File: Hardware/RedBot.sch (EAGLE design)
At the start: 67 parts, among them U1 ATMEGA328P, U2 TB6612FNG, U3 MIC5219 5V, U4 MIC5219 3.3V, U5 FT232RLSSOP, U6 7408SE, Y1 16MHz

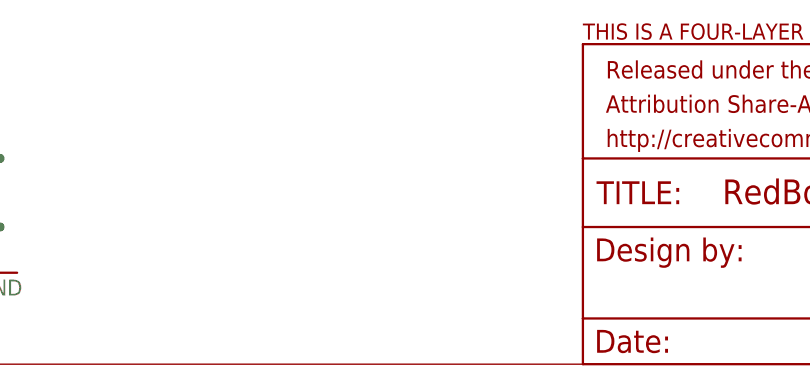
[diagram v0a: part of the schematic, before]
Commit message: Added RedBot logo
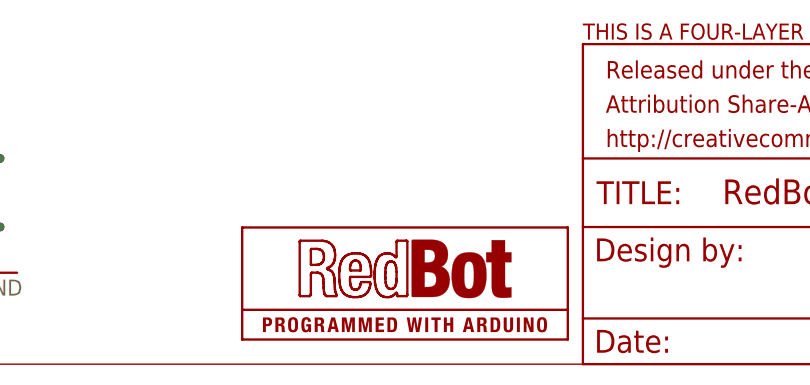
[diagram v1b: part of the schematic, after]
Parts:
- added U$23: REDBOT_LOGO, SparkFun-Aesthetics:REDBOT_LOGO
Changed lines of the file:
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@@
 <part name="S5" library="SparkFun-Electromechanical" deviceset="TAC_SWITCH" device="SMD"/>
 <part name="GND12" library="SparkFun-Aesthetics" deviceset="GND" device=""/>
+<part name="U$23" library="SparkFun-Aesthetics" deviceset="REDBOT_LOGO" device=""/>
 </parts>
 <sheets>
@@
 <instance part="S5" gate="S" x="309.88" y="93.98" rot="R90"/>
 <instance part="GND12" gate="1" x="309.88" y="83.82"/>
+<instance part="U$23" gate="G$1" x="266.7" y="2.54"/>
 </instances>
 <busses>

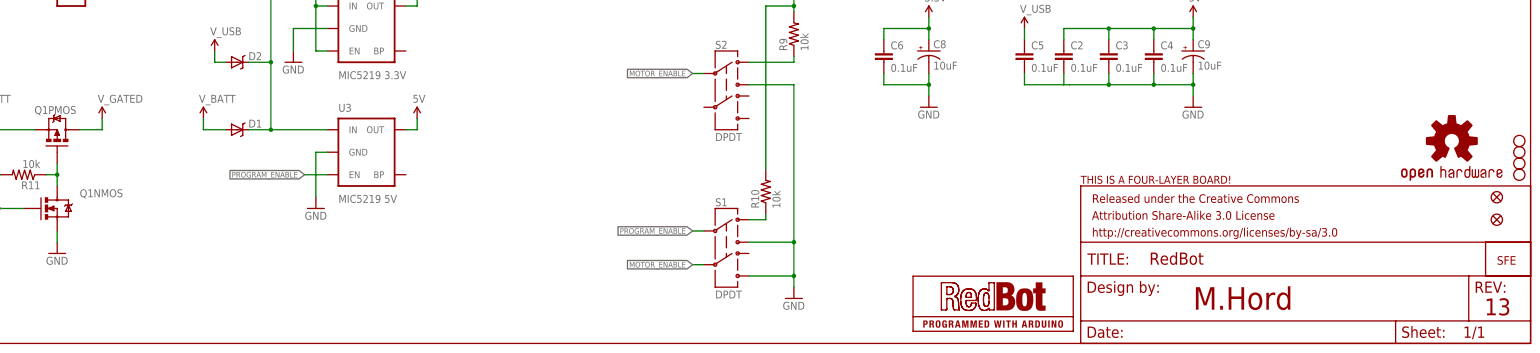
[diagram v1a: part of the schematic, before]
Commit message: Added PTC to V_GATED
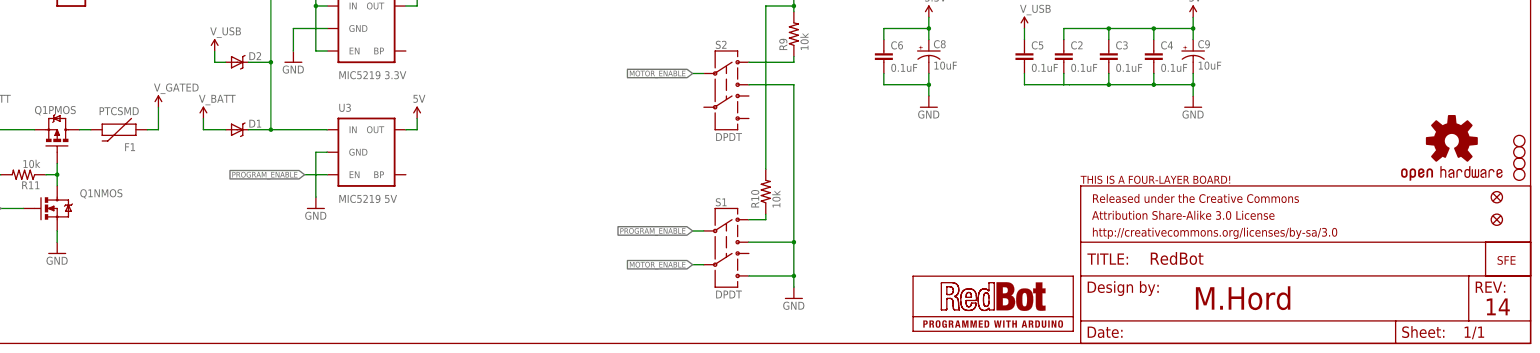
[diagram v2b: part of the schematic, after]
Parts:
- added F1: PTCSMD, SparkFun-PowerIC:PTCSMD
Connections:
- new net N$9: F1.2, Q1PMOS.D
- net V_GATED: now also F1.1; no longer Q1PMOS.D
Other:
- note added: "14"
- note removed: "13"
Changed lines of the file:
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@@
 <part name="GND12" library="SparkFun-Aesthetics" deviceset="GND" device=""/>
 <part name="U$23" library="SparkFun-Aesthetics" deviceset="REDBOT_LOGO" device=""/>
+<part name="F1" library="SparkFun-PowerIC" deviceset="PTC" device="SMD"/>
 </parts>
 <sheets>
@@
 <wire x1="0" y1="254" x2="0" y2="0" width="0.1524" layer="94"/>
 <text x="330.2" y="7.62" size="5.08" layer="94">M.Hord</text>
-<text x="395.986" y="6.35" size="3.81" layer="94">13</text>
+<text x="395.986" y="6.35" size="3.81" layer="94">14</text>
 </plain>
 <instances>
@@
 <instance part="U$18" gate="G$1" x="55.88" y="50.8"/>
 <instance part="GND20" gate="1" x="132.08" y="30.48"/>
-<instance part="V_GATE1" gate="G$1" x="83.82" y="50.8"/>
+<instance part="V_GATE1" gate="G$1" x="96.52" y="53.34"/>
 <instance part="U$4" gate="G$1" x="106.68" y="50.8"/>
 <instance part="JP16" gate="G$1" x="15.24" y="22.86"/>
@@
 <instance part="GND12" gate="1" x="309.88" y="83.82"/>
 <instance part="U$23" gate="G$1" x="266.7" y="2.54"/>
+<instance part="F1" gate="G$1" x="88.9" y="48.26" rot="R180"/>
 </instances>
 <busses>
@@
 <segment>
 <pinref part="V_GATE1" gate="G$1" pin="V_BATT"/>
-<wire x1="83.82" y1="50.8" x2="83.82" y2="48.26" width="0.1524" layer="91"/>
-<pinref part="Q1" gate="PMOS" pin="D"/>
-<wire x1="78.74" y1="48.26" x2="83.82" y2="48.26" width="0.1524" layer="91"/>
+<wire x1="96.52" y1="48.26" x2="96.52" y2="53.34" width="0.1524" layer="91"/>
+<pinref part="F1" gate="G$1" pin="1"/>
+<wire x1="93.98" y1="48.26" x2="96.52" y2="48.26" width="0.1524" layer="91"/>
 </segment>
 <segment>
@@
 </segment>
 </net>
+<net name="N$9" class="0">
+<segment>
+<pinref part="F1" gate="G$1" pin="2"/>
+<pinref part="Q1" gate="PMOS" pin="D"/>
+<wire x1="81.28" y1="48.26" x2="78.74" y2="48.26" width="0.1524" layer="91"/>
+</segment>
+</net>
